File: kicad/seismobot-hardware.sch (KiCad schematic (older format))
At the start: 98 parts, among them J1 Screw_Terminal_01x02, J2 Raspberry_Pi_2_3, U1 OPA2156xD, U10 AP7340, U2 OPA2156xD, U3 ref-6, U4 ref-8, U5 LTC6011, U6 OPA2156xD, U7 OPA2156xD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

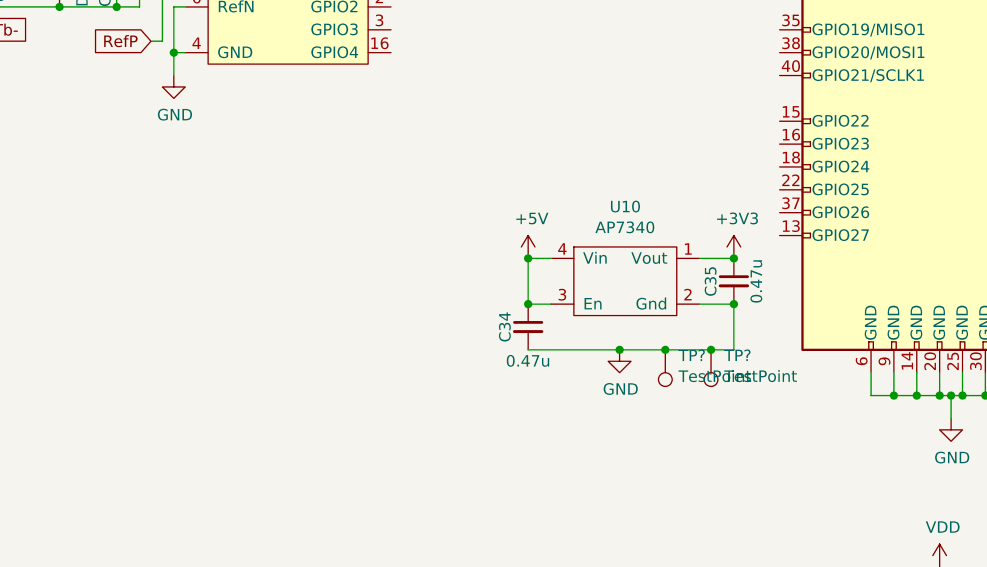
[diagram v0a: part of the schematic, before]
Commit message: add 3v3 power led
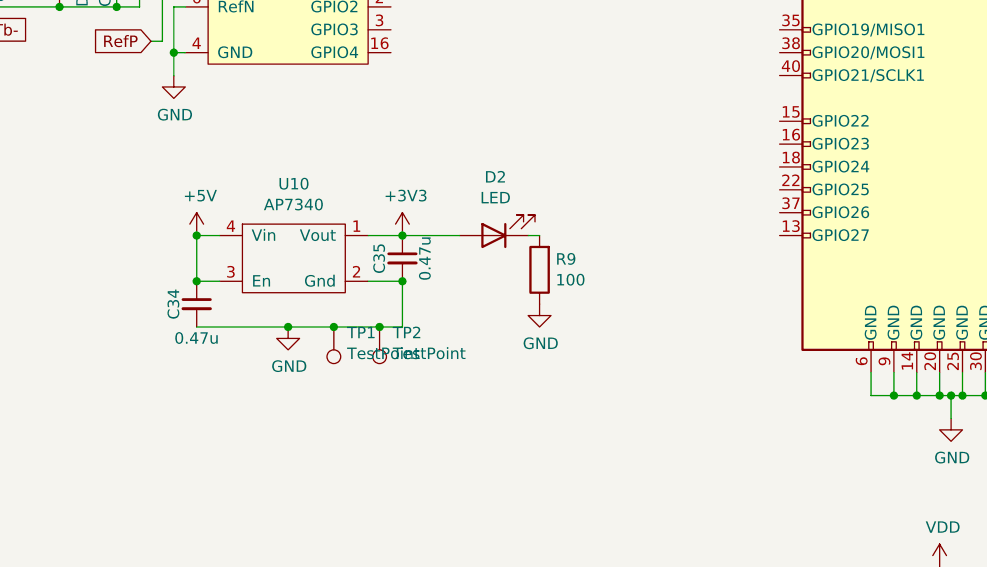
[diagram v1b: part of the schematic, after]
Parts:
- added D2: LED, LED_SMD:LED_0805_2012Metric, symbol Device:LED
- added R9: 100, Resistor_SMD:R_0805_2012Metric, symbol Device:R
- gave numbers to parts that had none: 2
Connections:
- net +3V3: now also D2.2 (A)
- net GND: now also R9.1
- new net: D2.1 (K), R9.2
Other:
- moved on the sheet: C34, C35, TP1, TP2, U10
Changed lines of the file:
@@
 L power:+3V3 #PWR0101
 U 1 1 60F23F5D
-P 8950 3150
-F 0 "#PWR0101" H 8950 3000 50  0001 C CNN
-F 1 "+3V3" H 8965 3323 50  0000 C CNN
-F 2 "" H 8950 3150 50  0001 C CNN
-F 3 "" H 8950 3150 50  0001 C CNN
-	1    8950 3150
+P 7500 3050
+F 0 "#PWR0101" H 7500 2900 50  0001 C CNN
+F 1 "+3V3" H 7515 3223 50  0000 C CNN
+F 2 "" H 7500 3050 50  0001 C CNN
+F 3 "" H 7500 3050 50  0001 C CNN
+	1    7500 3050
 	1    0    0    -1
 $EndComp
@@
 L power:+5V #PWR0102
 U 1 1 60F3CF53
-P 8050 3150
-F 0 "#PWR0102" H 8050 3000 50  0001 C CNN
-F 1 "+5V" H 8065 3323 50  0000 C CNN
-F 2 "" H 8050 3150 50  0001 C CNN
-F 3 "" H 8050 3150 50  0001 C CNN
-	1    8050 3150
+P 6600 3050
+F 0 "#PWR0102" H 6600 2900 50  0001 C CNN
+F 1 "+5V" H 6615 3223 50  0000 C CNN
+F 2 "" H 6600 3050 50  0001 C CNN
+F 3 "" H 6600 3050 50  0001 C CNN
+	1    6600 3050
 	1    0    0    -1
 $EndComp
@@
 L power:GND #PWR0103
 U 1 1 60F56154
-P 8450 3550
-F 0 "#PWR0103" H 8450 3300 50  0001 C CNN
-F 1 "GND" H 8455 3377 50  0000 C CNN
-F 2 "" H 8450 3550 50  0001 C CNN
-F 3 "" H 8450 3550 50  0001 C CNN
-	1    8450 3550
+P 7000 3450
+F 0 "#PWR0103" H 7000 3200 50  0001 C CNN
+F 1 "GND" H 7005 3277 50  0000 C CNN
+F 2 "" H 7000 3450 50  0001 C CNN
+F 3 "" H 7000 3450 50  0001 C CNN
+	1    7000 3450
 	1    0    0    -1
 $EndComp
@@
 L Device:C_Small C35
 U 1 1 60F5653E
-P 8950 3250
-F 0 "C35" V 9050 3250 50  0000 C CNN
-F 1 "0.47u" V 8850 3250 50  0000 C CNN
-F 2 "Capacitor_SMD:C_0805_2012Metric" H 8950 3250 50  0001 C CNN
-F 3 "~" H 8950 3250 50  0001 C CNN
-	1    8950 3250
+P 7500 3150
+F 0 "C35" V 7600 3150 50  0000 C CNN
+F 1 "0.47u" V 7400 3150 50  0000 C CNN
+F 2 "Capacitor_SMD:C_0805_2012Metric" H 7500 3150 50  0001 C CNN
+F 3 "~" H 7500 3150 50  0001 C CNN
+	1    7500 3150
 	-1   0    0    -1
 $EndComp
@@
 L Device:C_Small C34
 U 1 1 60F56DCF
-P 8050 3450
-F 0 "C34" V 8150 3450 50  0000 C CNN
-F 1 "0.47u" H 8050 3300 50  0000 C CNN
-F 2 "Capacitor_SMD:C_0805_2012Metric" H 8050 3450 50  0001 C CNN
-F 3 "~" H 8050 3450 50  0001 C CNN
-	1    8050 3450
-	-1   0    0    -1
-$EndComp
-Wire Wire Line
-	8050 3550 8450 3550
-Connection ~ 8450 3550
+P 6600 3350
+F 0 "C34" V 6700 3350 50  0000 C CNN
+F 1 "0.47u" H 6600 3200 50  0000 C CNN
+F 2 "Capacitor_SMD:C_0805_2012Metric" H 6600 3350 50  0001 C CNN
+F 3 "~" H 6600 3350 50  0001 C CNN
+	1    6600 3350
+	-1   0    0    -1
+$EndComp
+Wire Wire Line
+	6600 3450 7000 3450
+Connection ~ 7000 3450
 $Comp
 L power:VDD #PWR0104
@@
 L seismobot-hardware:AP7340 U10
 U 1 1 6139C2BB
-P 8500 3200
-F 0 "U10" H 8475 3475 50  0000 C CNN
-F 1 "AP7340" H 8475 3384 50  0000 C CNN
-F 2 "seismobot-hardware:DFN-1010-4" H 8500 3200 50  0001 C CNN
-F 3 "" H 8500 3200 50  0001 C CNN
-	1    8500 3200
-	1    0    0    -1
-$EndComp
-Wire Wire Line
-	8050 3150 8050 3350
-Wire Wire Line
-	8150 3150 8050 3150
-Connection ~ 8050 3150
-Wire Wire Line
-	8150 3350 8050 3350
-Connection ~ 8050 3350
-Wire Wire Line
-	8800 3150 8950 3150
-Connection ~ 8950 3150
-Wire Wire Line
-	8950 3350 8800 3350
-Wire Wire Line
-	8950 3550 8950 3350
-Wire Wire Line
-	8450 3550 8650 3550
-Connection ~ 8950 3350
-$Comp
-L Connector:TestPoint TP?
+P 7050 3100
+F 0 "U10" H 7025 3375 50  0000 C CNN
+F 1 "AP7340" H 7025 3284 50  0000 C CNN
+F 2 "seismobot-hardware:DFN-1010-4" H 7050 3100 50  0001 C CNN
+F 3 "" H 7050 3100 50  0001 C CNN
+	1    7050 3100
+	1    0    0    -1
+$EndComp
+Wire Wire Line
+	6600 3050 6600 3250
+Wire Wire Line
+	6700 3050 6600 3050
+Connection ~ 6600 3050
+Wire Wire Line
+	6700 3250 6600 3250
+Connection ~ 6600 3250
+Wire Wire Line
+	7350 3050 7500 3050
+Connection ~ 7500 3050
+Wire Wire Line
+	7500 3250 7350 3250
+Wire Wire Line
+	7500 3450 7500 3250
+Wire Wire Line
+	7000 3450 7200 3450
+Connection ~ 7500 3250
+$Comp
+L Connector:TestPoint TP2
 U 1 1 6146A6B1
-P 8850 3550
-F 0 "TP?" H 8792 3576 50  0000 R CNN
-F 1 "TestPoint" H 8792 3667 50  0000 R CNN
-F 2 "Connector_PinHeader_2.54mm:PinHeader_1x01_P2.54mm_Vertical" H 9050 3550 50  0001 C CNN
-F 3 "~" H 9050 3550 50  0001 C CNN
-	1    8850 3550
+P 7400 3450
+F 0 "TP2" H 7342 3476 50  0000 R CNN
+F 1 "TestPoint" H 7342 3567 50  0000 R CNN
+F 2 "Connector_PinHeader_2.54mm:PinHeader_1x01_P2.54mm_Vertical" H 7600 3450 50  0001 C CNN
+F 3 "~" H 7600 3450 50  0001 C CNN
+	1    7400 3450
 	-1   0    0    1
 $EndComp
 $Comp
-L Connector:TestPoint TP?
+L Connector:TestPoint TP1
 U 1 1 6146B4AA
-P 8650 3550
-F 0 "TP?" H 8592 3576 50  0000 R CNN
-F 1 "TestPoint" H 8592 3667 50  0000 R CNN
-F 2 "Connector_PinHeader_2.54mm:PinHeader_1x01_P2.54mm_Vertical" H 8850 3550 50  0001 C CNN
-F 3 "~" H 8850 3550 50  0001 C CNN
-	1    8650 3550
+P 7200 3450
+F 0 "TP1" H 7142 3476 50  0000 R CNN
+F 1 "TestPoint" H 7142 3567 50  0000 R CNN
+F 2 "Connector_PinHeader_2.54mm:PinHeader_1x01_P2.54mm_Vertical" H 7400 3450 50  0001 C CNN
+F 3 "~" H 7400 3450 50  0001 C CNN
+	1    7200 3450
 	-1   0    0    1
 $EndComp
-Connection ~ 8850 3550
-Wire Wire Line
-	8850 3550 8950 3550
-Connection ~ 8650 3550
-Wire Wire Line
-	8650 3550 8850 3550
+Connection ~ 7400 3450
+Wire Wire Line
+	7400 3450 7500 3450
+Connection ~ 7200 3450
+Wire Wire Line
+	7200 3450 7400 3450
+$Comp
+L Device:LED D2
+U 1 1 60DFF3AF
+P 7900 3050
+F 0 "D2" H 7893 2795 50  0000 C CNN
+F 1 "LED" H 7893 2886 50  0000 C CNN
+F 2 "LED_SMD:LED_0805_2012Metric" H 7900 3050 50  0001 C CNN
+F 3 "~" H 7900 3050 50  0001 C CNN
+	1    7900 3050
+	-1   0    0    1
+$EndComp
+$Comp
+L Device:R R9
+U 1 1 60DFF3B5
+P 8100 3200
+F 0 "R9" H 8030 3154 50  0000 R CNN
+F 1 "100" H 8030 3245 50  0000 R CNN
+F 2 "Resistor_SMD:R_0805_2012Metric" V 8030 3200 50  0001 C CNN
+F 3 "~" H 8100 3200 50  0001 C CNN
+	1    8100 3200
+	-1   0    0    1
+$EndComp
+Wire Wire Line
+	8050 3050 8100 3050
+Wire Wire Line
+	7500 3050 7750 3050
+$Comp
+L power:GND #PWR0112
+U 1 1 60E37B62
+P 8100 3350
+F 0 "#PWR0112" H 8100 3100 50  0001 C CNN
+F 1 "GND" H 8105 3177 50  0000 C CNN
+F 2 "" H 8100 3350 50  0001 C CNN
+F 3 "" H 8100 3350 50  0001 C CNN
+	1    8100 3350
+	1    0    0    -1
+$EndComp
 $EndSCHEMATC

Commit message: finishing touches before sending out rev 1
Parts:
- added J3: Conn_01x06_Male, Connector_PinHeader_2.54mm:PinHeader_1x06_P2.54mm_Horizontal, symbol Connector:Conn_01x06_Male
- added R14: DNP, Resistor_SMD:R_0805_2012Metric, symbol Device:R_Small_US
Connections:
- net G+: now also R14.2
- net G-: now also R14.1
- net GND: now also J3.3 (Pin_3), J3.6 (Pin_6)
- net SWCLK: now also J3.2 (Pin_2)
- net SWDIO: now also J3.4 (Pin_4)
- net VDD: now also J3.1 (Pin_1)
- net ~RST: now also J3.5 (Pin_5)
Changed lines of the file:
@@
 $EndComp
 Wire Wire Line
-	850  6700 1100 6700
+	850  6700 900  6700
 Text Notes 550  1150 0    50   ~ 0
 Negative Input
@@
 	1100 6700 1100 6800
 Wire Wire Line
-	850  7100 1100 7100
+	850  7100 900  7100
 Wire Wire Line
 	1100 7000 1100 7100
@@
 	1    0    0    -1
 $EndComp
+$Comp
+L Connector:Conn_01x06_Male J3
+U 1 1 60E4F5E6
+P 8450 4250
+F 0 "J3" H 8558 4631 50  0000 C CNN
+F 1 "Conn_01x06_Male" H 8558 4540 50  0000 C CNN
+F 2 "Connector_PinHeader_2.54mm:PinHeader_1x06_P2.54mm_Horizontal" H 8450 4250 50  0001 C CNN
+F 3 "~" H 8450 4250 50  0001 C CNN
+	1    8450 4250
+	1    0    0    -1
+$EndComp
+$Comp
+L power:VDD #PWR0113
+U 1 1 60E5097B
+P 8950 4050
+F 0 "#PWR0113" H 8950 3900 50  0001 C CNN
+F 1 "VDD" H 8965 4223 50  0000 C CNN
+F 2 "" H 8950 4050 50  0001 C CNN
+F 3 "" H 8950 4050 50  0001 C CNN
+	1    8950 4050
+	1    0    0    -1
+$EndComp
+Wire Wire Line
+	8650 4050 8950 4050
+Text GLabel 8950 4150 2    50   Input ~ 0
+SWCLK
+Wire Wire Line
+	8650 4150 8950 4150
+$Comp
+L power:GND #PWR0114
+U 1 1 60E8AE9A
+P 9300 4250
+F 0 "#PWR0114" H 9300 4000 50  0001 C CNN
+F 1 "GND" H 9305 4077 50  0000 C CNN
+F 2 "" H 9300 4250 50  0001 C CNN
+F 3 "" H 9300 4250 50  0001 C CNN
+	1    9300 4250
+	1    0    0    -1
+$EndComp
+Wire Wire Line
+	8650 4250 9300 4250
+Text GLabel 8950 4350 2    50   Input ~ 0
+SWDIO
+Wire Wire Line
+	8650 4350 8950 4350
+Text GLabel 9000 4500 2    50   Input ~ 0
+~RST
+Wire Wire Line
+	8650 4450 8950 4450
+Wire Wire Line
+	8950 4450 8950 4500
+Wire Wire Line
+	8950 4500 9000 4500
+$Comp
+L power:GND #PWR0115
+U 1 1 60F1D12E
+P 8850 4550
+F 0 "#PWR0115" H 8850 4300 50  0001 C CNN
+F 1 "GND" H 8855 4377 50  0000 C CNN
+F 2 "" H 8850 4550 50  0001 C CNN
+F 3 "" H 8850 4550 50  0001 C CNN
+	1    8850 4550
+	1    0    0    -1
+$EndComp
+Wire Wire Line
+	8650 4550 8850 4550
+Wire Wire Line
+	900  6700 900  6800
+Connection ~ 900  6700
+Wire Wire Line
+	900  6700 1100 6700
+Wire Wire Line
+	900  7000 900  7100
+Connection ~ 900  7100
+Wire Wire Line
+	900  7100 1100 7100
+$Comp
+L Device:R_Small_US R14
+U 1 1 610155EF
+P 900 6900
+F 0 "R14" V 1000 6800 50  0000 C CNN
+F 1 "DNP" V 1000 6950 50  0000 C CNN
+F 2 "Resistor_SMD:R_0805_2012Metric" H 900 6900 50  0001 C CNN
+F 3 "~" H 900 6900 50  0001 C CNN
+	1    900  6900
+	-1   0    0    1
+$EndComp
 $EndSCHEMATC

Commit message: re-arrange schematic for aesthetics, add Title Block
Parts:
- U1, U2, U5, U6, U7: symbol Amplifier_Operational:OPA2156xD -> seismobot-hardware-rescue:OPA2156xD-Amplifier_Operational
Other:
- moved on the sheet: C1, C10, C11, C12, C13, C14, C15, C16, C17, C18, C19, C2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
